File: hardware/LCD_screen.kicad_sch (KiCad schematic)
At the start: 4 parts, among them U300 BU9797A

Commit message: Routing close to completion. Pending review.
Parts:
- added TP500: ~, TestPoint:TestPoint_Pad_D1.0mm, symbol Connector:TestPoint
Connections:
- net at C2.1, RV1.2, U300.11 (VDD): now also TP500.1
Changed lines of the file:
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@@
+    )
+  )
+  (symbol (lib_id "Connector:TestPoint") (at 55.88 57.15 0) (unit 1)
+    (in_bom yes) (on_board yes) (dnp no) (fields_autoplaced)
+    (property "Reference" "TP500" (at 57.785 54.483 0)
+      (effects (font (size 1.27 1.27)) (justify left))
+    )
+    (property "Value" "~" (at 57.785 55.753 0)
+      (effects (font (size 1.27 1.27)) (justify left))
+    )
+    (property "Footprint" "TestPoint:TestPoint_Pad_D1.0mm" (at 60.96 57.15 0)
+      (effects (font (size 1.27 1.27)) hide)
+    )
+    (property "Datasheet" "~" (at 60.96 57.15 0)
+      (effects (font (size 1.27 1.27)) hide)
+    )
+    (pin "1")
+    (instances
+      (project "current_sink_dev"
+        (path "/695b42ec-77e0-4be3-bf4d-1fc5cfcb9ef1/02451f10-14c4-4640-81bd-2617f523efcf"
+          (reference "TP500") (unit 1)
+        )
+        (path "/695b42ec-77e0-4be3-bf4d-1fc5cfcb9ef1/799b6aec-5164-443b-a573-074aa3713aa0"
+          (reference "TP507") (unit 1)
+        )
+      )
     )
   )

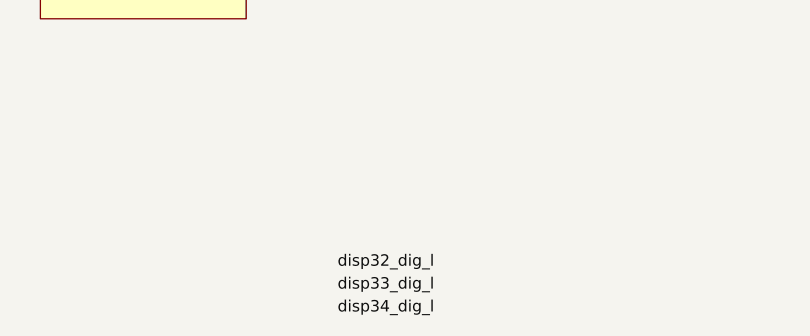
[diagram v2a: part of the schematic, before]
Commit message: Started programming LCD interface
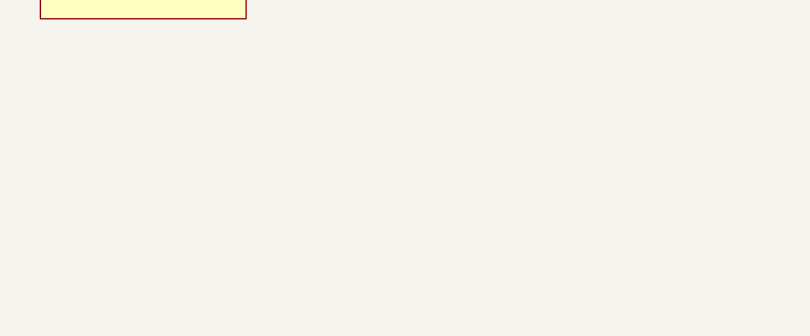
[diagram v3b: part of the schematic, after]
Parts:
- U300: footprint Package_SO:TSSOP-48_8x12.5mm_P0.5mm -> Package_SO:TSSOP-48_6.1x12.5mm_P0.5mm
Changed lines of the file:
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@@
-    (effects (font (size 1.27 1.27)) (justify left bottom))
-  )
-  (label "disp33_dig_l" (at 111.76 204.47 0) (fields_autoplaced)
     (effects (font (size 1.27 1.27)) (justify left bottom))
   )
@@
     (effects (font (size 1.27 1.27)) (justify left bottom))
   )
-  (label "disp32_dig_l" (at 111.76 201.93 0) (fields_autoplaced)
-    (effects (font (size 1.27 1.27)) (justify left bottom))
-  )
   (label "disp31_dig_l" (at 228.6 77.47 0) (fields_autoplaced)
     (effects (font (size 1.27 1.27)) (justify left bottom))
@@
   )
   (label "COM2_dig_l" (at 115.57 165.1 0) (fields_autoplaced)
-    (effects (font (size 1.27 1.27)) (justify left bottom))
-  )
-  (label "disp34_dig_l" (at 111.76 207.01 0) (fields_autoplaced)
     (effects (font (size 1.27 1.27)) (justify left bottom))
   )
@@
       (effects (font (size 1.27 1.27)))
     )
-    (property "Footprint" "Package_SO:TSSOP-48_8x12.5mm_P0.5mm" (at 90.17 53.34 0)
-      (effects (font (size 1.27 1.27)) hide)
-    )
+    (property "Footprint" "Package_SO:TSSOP-48_6.1x12.5mm_P0.5mm" (at 90.17 53.34 0)
+      (effects (font (size 1.27 1.27)) hide)
+    )

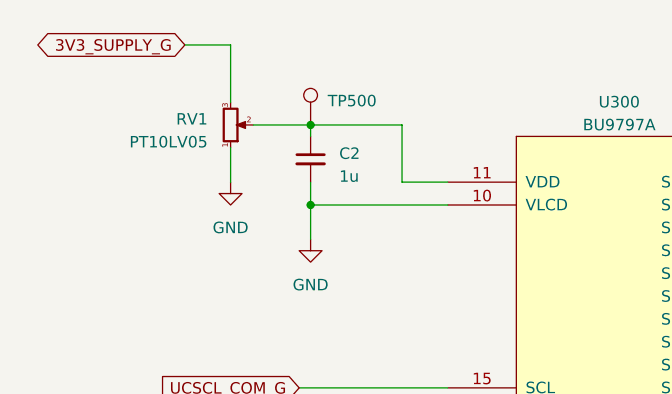
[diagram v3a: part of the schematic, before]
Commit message: Added some doucmentation to MCP driver
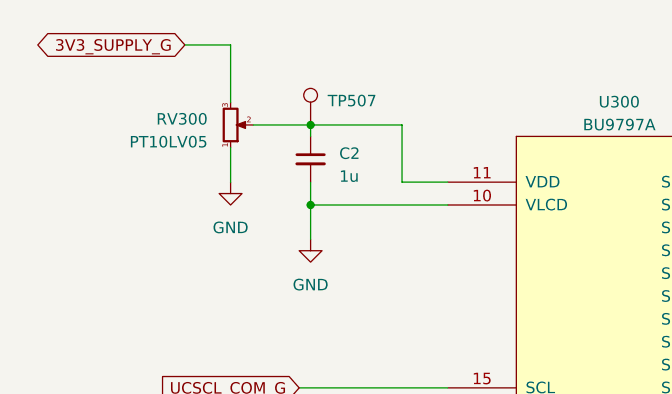
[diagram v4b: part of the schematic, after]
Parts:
- renumbered RV1 to RV300, TP500 to TP507
